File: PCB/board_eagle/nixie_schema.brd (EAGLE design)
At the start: 200 x 160 mm, 55 parts, among them IC1 LM2672M

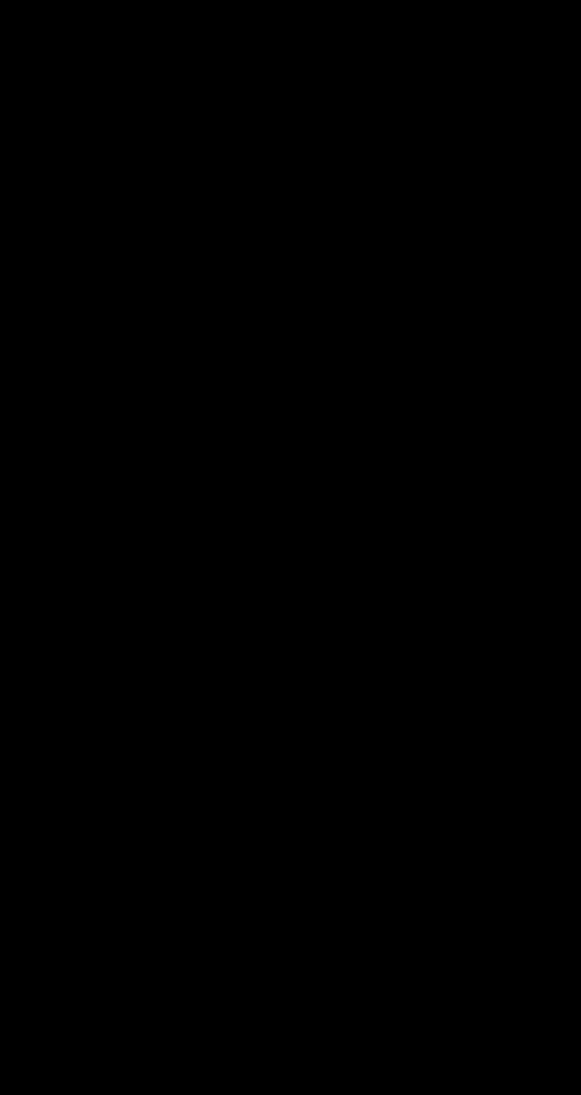
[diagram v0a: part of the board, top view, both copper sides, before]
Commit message: Fixing minor schematic issues (anode resistors and cap values in 3v3 PSU). Updated gitignore with EAGLE temp files
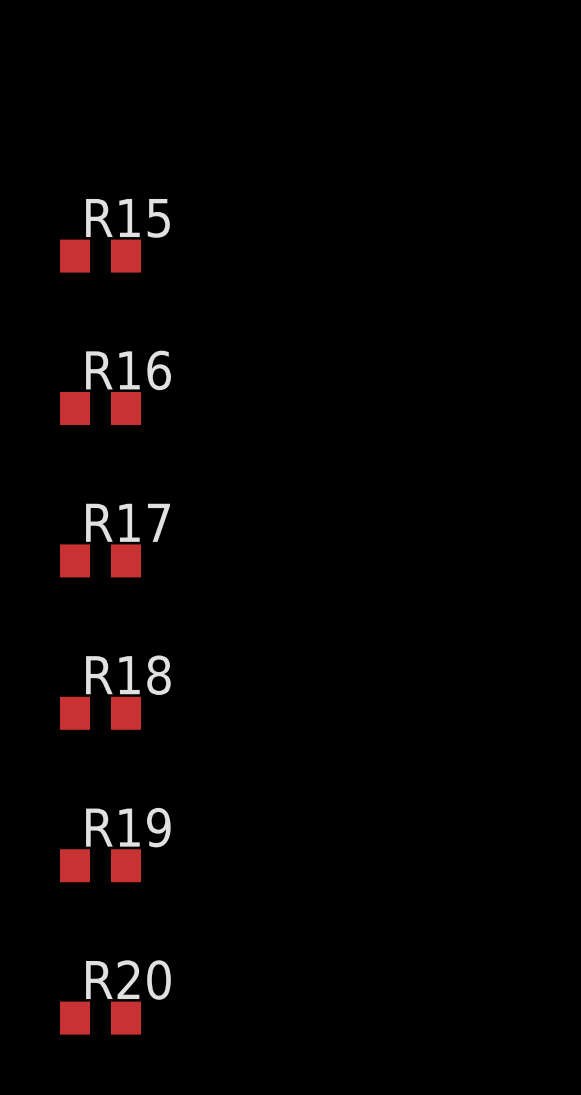
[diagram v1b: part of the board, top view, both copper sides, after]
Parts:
- added R15, R16, R17, R18, R19, R20: (no value), resistor:R0603
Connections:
- removed net N$74: N1.A, N2.A, N3.A, N4.A, N5.A, N6.A, SV10.11, SV10.12, SV11.11, SV11.12, SV12.11, SV12.12, SV7.11, SV7.12, SV8.11, SV8.12, SV9.11, SV9.12
- new net N$45: R15.2, R16.2, R17.2, R18.2, R19.2, R20.2, SV10.11, SV10.12, SV11.11, SV11.12, SV12.11, SV12.12, SV7.11, SV7.12, SV8.11, SV8.12, SV9.11, SV9.12
- new net N$89: N6.A, R20.1
- new net N$90: N5.A, R19.1
- new net N$91: N4.A, R18.1
- new net N$92: N3.A, R17.1
- new net N$93: N2.A, R16.1
- new net N$94: N1.A, R15.1
- net GND: now also C6.1; no longer C5.1
- net N$11: now also C5.1; no longer C6.1
- net N$12: now also C5.2; no longer C6.2
- net N$5: now also C6.2; no longer C5.2

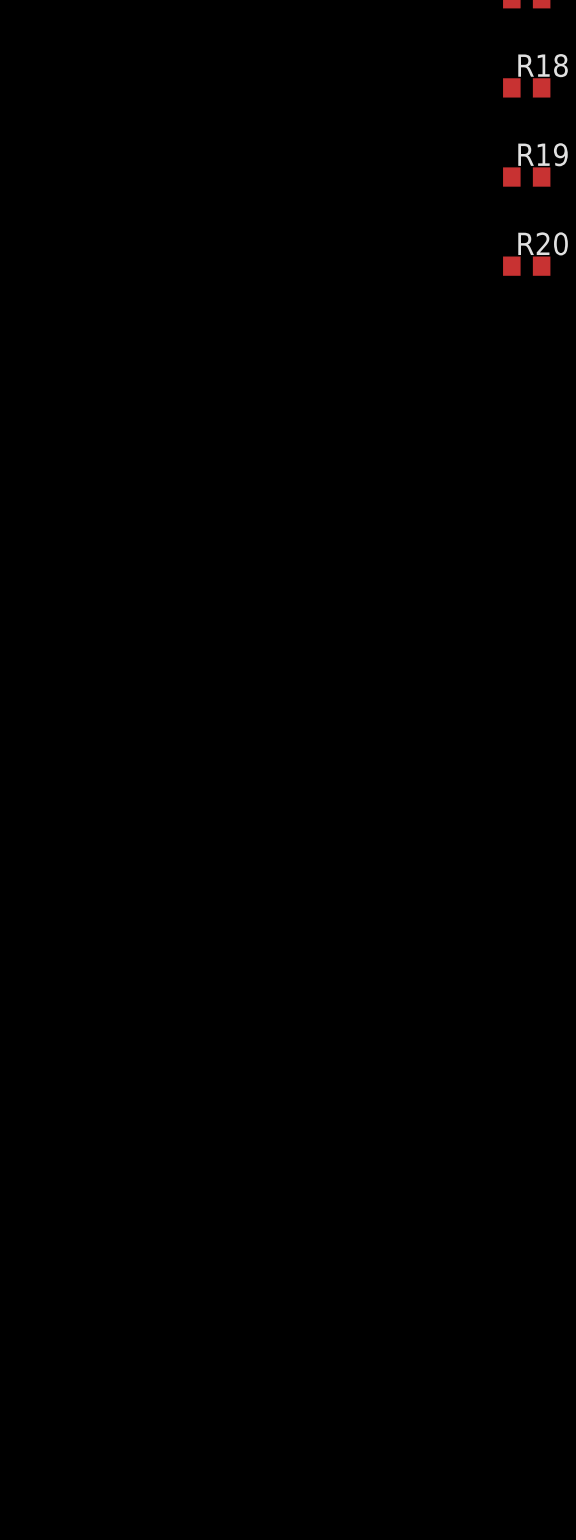
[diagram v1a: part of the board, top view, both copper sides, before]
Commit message: Most of HV supply schematic done. Need to pick transistors, caps and diode
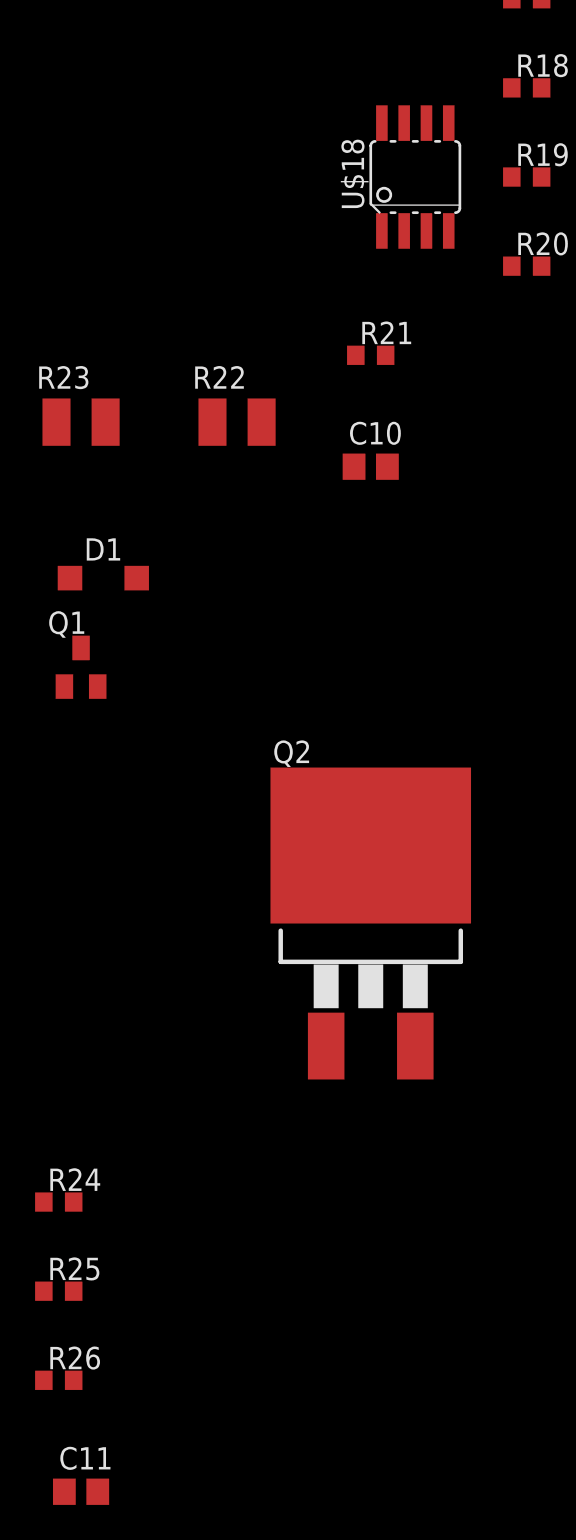
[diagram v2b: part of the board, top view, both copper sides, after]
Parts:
- added C10, C11: 680p, eagle-ltspice:C0805
- added D1: (no value), diode:SOD123
- added Q1: (no value), semicon-smd-ipc:SOT23
- added Q2: IRF3704S, transistor-power:D2PACK
- added R21: 1k, resistor:R0603
- added R22, R23: (no value), eagle-ltspice:R1210
- added R24: 330k, resistor:R0603
- added R25: 3.3k, resistor:R0603
- added R26: 5.6k, resistor:R0603
- added U$18: MC34063, MC34063:SOIC08
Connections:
- new net N$74: C10.1, U$18.3
- new net N$85: D1.A, Q1.1, R21.1, U$18.2
- new net N$86: Q2.2
- new net N$87: R22.2, R23.2, U$18.1, U$18.7, U$18.8
- new net N$95: D1.C, Q1.2, Q2.1
- new net N$96: C11.1, R24.2, R25.1, R26.1, U$18.5
- new net N$97: R26.2
- net GND: now also C10.2, C11.2, Q1.3, Q2.3, R21.2, R25.2, U$18.4
- net HV_IN+: now also R24.1
- net VCC: now also R22.1, R23.1, U$18.6

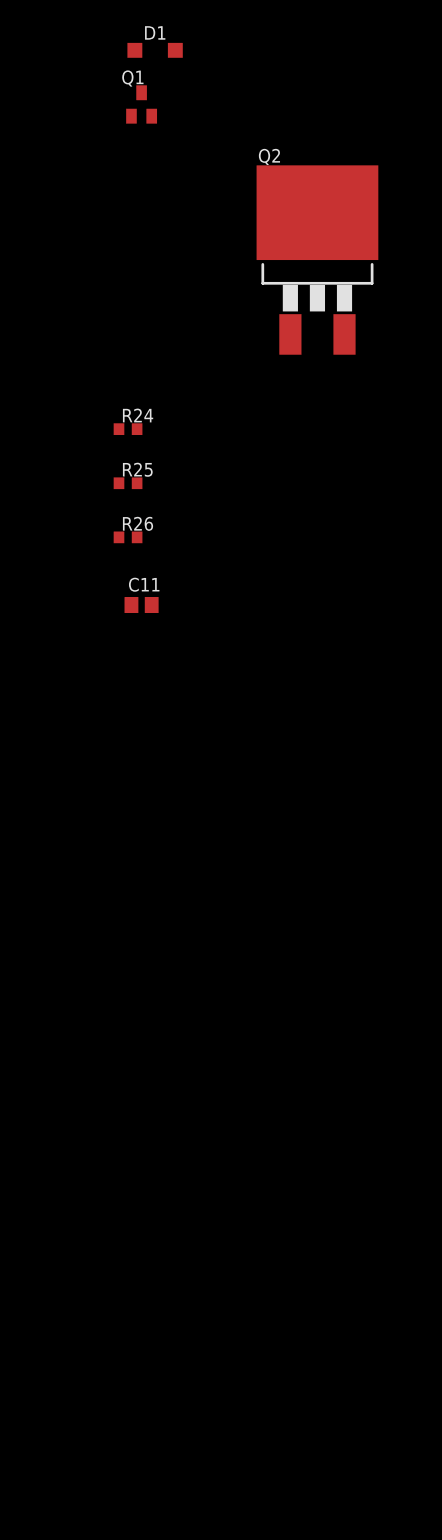
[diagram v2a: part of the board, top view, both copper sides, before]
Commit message: HV PSU schematic captured. Still need to pick correct pot
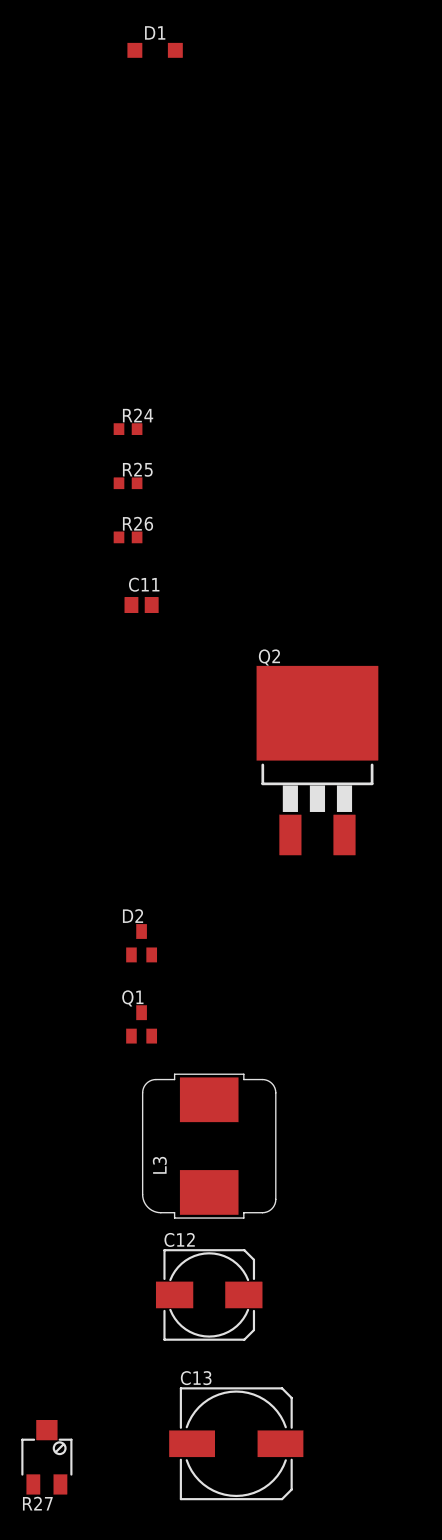
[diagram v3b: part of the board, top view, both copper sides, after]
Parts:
- added C12: 220u, rcl:153CLV-0810
- added C13: 2.2u, rcl:153CLV-1014
- added D2: BAS21, nixe_cmp:SOT23
- added L3: 150u, nixe_cmp:INDUCTOR_PACKAGE
- added R27: 100k, pot:SM-42/43X
- Q1: value (none) -> BC856B; device semicon-smd-ipc:SOT23 -> nixe_cmp:SOT23
- Q2: value IRF3704S -> IRF740S; device transistor-power:D2PACK -> nixe_cmp:D2PACK
- moved Q1 86.4 mm to (-106.7, -222.2)
- moved Q2 47.0 mm to (-90.2, -195.6)
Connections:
- net GND: now also C12.-, C13.-, R27.2
- net HV_IN+: now also C13.+, D2.3
- net N$86: now also D2.1, L3.P$2
- net N$87: now also C12.+, L3.P$1
- net N$97: now also R27.3
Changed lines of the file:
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@@
 </element>
 <element name="D1" library="diode" package="SOD123" value="" x="-105.41" y="-130.81"/>
-<element name="Q1" library="semicon-smd-ipc" package="SOT23" value="" x="-106.68" y="-135.89"/>
-<element name="Q2" library="transistor-power" package="D2PACK" value="IRF3704S" x="-90.17" y="-148.59"/>
 <element name="R24" library="resistor" package="R0603" value="330k" x="-107.95" y="-166.37"/>
 <element name="R25" library="resistor" package="R0603" value="3.3k" x="-107.95" y="-171.45"/>
@@
 <attribute name="SPICEPREFIX" value="C" x="-106.68" y="-182.88" size="1.778" layer="27" display="off"/>
 </element>
+<element name="Q2" library="nixe_cmp" package="D2PACK" value="IRF740S" x="-90.17" y="-195.58"/>
+<element name="D2" library="nixe_cmp" package="SOT23" value="BAS21" x="-106.68" y="-214.63"/>
+<element name="Q1" library="nixe_cmp" package="SOT23" value="BC856B" x="-106.68" y="-222.25"/>
+<element name="L3" library="nixe_cmp" package="INDUCTOR_PACKAGE" value="150u" x="-100.33" y="-233.68"/>
+<element name="C12" library="rcl" package="153CLV-0810" value="220u" x="-100.33" y="-247.65"/>
+<element name="C13" library="rcl" package="153CLV-1014" value="2.2u" x="-97.79" y="-261.62"/>
+<element name="R27" library="pot" package="SM-42/43X" value="100k" x="-115.57" y="-262.89"/>
 </elements>
 <signals>
@@
 <contactref element="C10" pad="2"/>
 <contactref element="R21" pad="2"/>
-<contactref element="Q1" pad="3"/>
-<contactref element="Q2" pad="3"/>
 <contactref element="R25" pad="2"/>
 <contactref element="C11" pad="2"/>
-<wire x1="-107.1" y1="-171.45" x2="-87.63" y2="-157.48" width="0" layer="19" extent="1-1"/>
-<wire x1="-105.73" y1="-182.88" x2="-107.1" y2="-171.45" width="0" layer="19" extent="1-1"/>
-<wire x1="-106.68" y1="-134.79" x2="-87.63" y2="-157.48" width="0" layer="19" extent="1-1"/>
-<wire x1="-89.22" y1="-124.46" x2="-106.68" y2="-134.79" width="0" layer="19" extent="1-1"/>
+<contactref element="Q2" pad="3"/>
+<contactref element="Q1" pad="3"/>
+<contactref element="C12" pad="-"/>
+<contactref element="C13" pad="-"/>
+<contactref element="R27" pad="2"/>
 <wire x1="-89.32" y1="-118.11" x2="-89.22" y2="-124.46" width="0" layer="19" extent="1-1"/>
 <wire x1="-85.725" y1="-111.0234" x2="-89.32" y2="-118.11" width="0" layer="19" extent="1-1"/>
+<wire x1="-107.1" y1="-171.45" x2="-89.22" y2="-124.46" width="0" layer="19" extent="1-1"/>
+<wire x1="-105.73" y1="-182.88" x2="-107.1" y2="-171.45" width="0" layer="19" extent="1-1"/>
+<wire x1="-87.63" y1="-204.47" x2="-105.73" y2="-182.88" width="0" layer="19" extent="1-1"/>
+<wire x1="-106.68" y1="-221.15" x2="-87.63" y2="-204.47" width="0" layer="19" extent="1-1"/>
+<wire x1="-103.58" y1="-247.65" x2="-106.68" y2="-221.15" width="0" layer="19" extent="1-1"/>
+<wire x1="-101.94" y1="-261.62" x2="-103.58" y2="-247.65" width="0" layer="19" extent="1-1"/>
+<wire x1="-115.57" y1="-260.34" x2="-101.94" y2="-261.62" width="0" layer="19" extent="1-1"/>
 <wire x1="-76.91" y1="55.88" x2="-85.725" y2="-111.0234" width="0" layer="19" extent="1-1"/>
 <wire x1="-64.21" y1="55.88" x2="-76.91" y2="55.88" width="0" layer="19" extent="1-1"/>
@@
 <contactref element="SV6" pad="12"/>
 <contactref element="R24" pad="1"/>
+<contactref element="D2" pad="3"/>
+<contactref element="C13" pad="+"/>
 <wire x1="186.35" y1="58.73" x2="186.35" y2="61.27" width="0" layer="19" extent="1-1"/>
 <wire x1="166.35" y1="61.27" x2="186.35" y2="61.27" width="0" layer="19" extent="1-1"/>
@@
 <wire x1="26.35" y1="58.73" x2="26.35" y2="61.27" width="0" layer="19" extent="1-1"/>
 <wire x1="-108.8" y1="-166.37" x2="26.35" y2="58.73" width="0" layer="19" extent="1-1"/>
+<wire x1="-106.68" y1="-213.53" x2="-108.8" y2="-166.37" width="0" layer="19" extent="1-1"/>
+<wire x1="-93.64" y1="-261.62" x2="-106.68" y2="-213.53" width="0" layer="19" extent="1-1"/>
 </signal>
 <signal name="HV_HA_0">
@@
 <contactref element="D1" pad="A"/>
 <contactref element="Q1" pad="1"/>
-<wire x1="-103.51" y1="-130.81" x2="-107.63" y2="-136.99" width="0" layer="19" extent="1-1"/>
 <wire x1="-91.02" y1="-118.11" x2="-103.51" y2="-130.81" width="0" layer="19" extent="1-1"/>
 <wire x1="-88.265" y1="-111.0234" x2="-91.02" y2="-118.11" width="0" layer="19" extent="1-1"/>
+<wire x1="-107.63" y1="-223.35" x2="-103.51" y2="-130.81" width="0" layer="19" extent="1-1"/>
 </signal>
 <signal name="N$87">
@@
 <contactref element="U$18" pad="8"/>
 <contactref element="U$18" pad="1"/>
+<contactref element="L3" pad="P$1"/>
+<contactref element="C12" pad="+"/>
 <wire x1="-96.39" y1="-121.92" x2="-105.28" y2="-121.92" width="0" layer="19" extent="1-1"/>
 <wire x1="-89.535" y1="-111.0234" x2="-96.39" y2="-121.92" width="0" layer="19" extent="1-1"/>
 <wire x1="-89.535" y1="-104.8766" x2="-89.535" y2="-111.0234" width="0" layer="19" extent="1-1"/>
 <wire x1="-88.265" y1="-104.8766" x2="-89.535" y2="-104.8766" width="0" layer="19" extent="1-1"/>
+<wire x1="-100.33" y1="-229.33" x2="-96.39" y2="-121.92" width="0" layer="19" extent="1-1"/>
+<wire x1="-97.08" y1="-247.65" x2="-100.33" y2="-229.33" width="0" layer="19" extent="1-1"/>
 </signal>
 <signal name="N$95">
-<contactref element="Q1" pad="2"/>
 <contactref element="D1" pad="C"/>
 <contactref element="Q2" pad="1"/>
-<wire x1="-105.73" y1="-136.99" x2="-92.71" y2="-157.48" width="0" layer="19" extent="1-1"/>
-<wire x1="-107.31" y1="-130.81" x2="-105.73" y2="-136.99" width="0" layer="19" extent="1-1"/>
+<contactref element="Q1" pad="2"/>
+<wire x1="-92.71" y1="-204.47" x2="-107.31" y2="-130.81" width="0" layer="19" extent="1-1"/>
+<wire x1="-105.73" y1="-223.35" x2="-92.71" y2="-204.47" width="0" layer="19" extent="1-1"/>
 </signal>
 <signal name="N$96">
@@
 <wire x1="-107.63" y1="-182.88" x2="-108.8" y2="-176.53" width="0" layer="19" extent="1-1"/>
 </signal>
+<signal name="N$97">
+<contactref element="R26" pad="2"/>
+<contactref element="R27" pad="3"/>
+<wire x1="-107.1" y1="-176.53" x2="-114.3" y2="-265.44" width="0" layer="19" extent="1-1"/>
+</signal>
 <signal name="N$86">
 <contactref element="Q2" pad="2"/>
-</signal>
-<signal name="N$97">
-<contactref element="R26" pad="2"/>
+<contactref element="D2" pad="1"/>
+<contactref element="L3" pad="P$2"/>
+<wire x1="-107.63" y1="-215.73" x2="-100.33" y2="-238.03" width="0" layer="19" extent="1-1"/>
+<wire x1="-90.17" y1="-193.04" x2="-107.63" y2="-215.73" width="0" layer="19" extent="1-1"/>
 </signal>
 </signals>

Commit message: Added Buttons
Added 4 buttons and two strip for connectors. buttons are on the last
alb gpios. removed connections for DOT_LED
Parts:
- added J3: (no value), SparkFun-Connectors:1X06_NO_SILK
- added R28, R29, R30: 2.21K, rcl:R0603
- added S2, S3, S4, S5: TAC_SWITCHSMD, SparkFun-Retired:TACTILE-SWITCH-SMD
- J2: device SparkFun-Connectors:1X03 -> SparkFun-Connectors:1X06_NO_SILK
- R7: value 150 -> 2.21K
- moved J2 430.5 mm to (-109.2, -344.2), turned to 0 degrees
- moved R7 408.5 mm to (-116.8, -316.2)
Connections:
- removed net DOT_LED: R7.1, U$13.G4
- removed net N$10: J2.2, R7.2
- removed net N$19: U$13.G12
- removed net N$21: U$13.G13
- new net BUTTON1: J2.2, J3.2, R30.2, S5.1, S5.2, U$13.G4
- new net BUTTON2: J2.3, J3.3, R29.2, S4.1, S4.2, U$13.G2
- new net BUTTON3: J2.4, J3.4, R28.2, S3.1, S3.2, U$13.G12
- new net BUTTON4: J2.5, J3.5, R7.2, S2.1, S2.2, U$13.G13
- net +3V3: now also J3.1, S2.3, S3.3, S4.3, S5.3
- net GND: now also J2.6, J3.6, R28.1, R29.1, R30.1, R7.1; no longer J2.3

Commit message: Changed ESP8266
changed esp8266 footprint
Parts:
- removed U$13: ESP8266-07-12, PatternAgents_RFmodules:ESP8266-07W
- added U1: (no value), PatternAgents_RFmodules:ESP12E-SMD
- S1: value MOMENTARY-SWITCH-SPST-SMD-4.5MM -> TAC_SWITCHSMD; device SparkFun-Switches:TACTILE_SWITCH_SMD_4.5MM -> SparkFun-Retired:TACTILE-SWITCH-SMD
- moved S1 438.6 mm to (-113.0, -356.9)
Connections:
- net +3V3: now also U1.VCC; no longer U$13.VCC
- net BUTTON1: now also U1.GPIO5; no longer U$13.G4
- net BUTTON2: now also U1.GPIO2; no longer U$13.G2
- net BUTTON3: now also U1.GPIO12; no longer U$13.G12
- net BUTTON4: now also U1.GPIO13; no longer U$13.G13
- net DATA_CLK: now also U1.GPIO14; no longer U$13.G14
- net DATA_IN: now also U1.GPIO16; no longer U$13.G16
- net GND: now also U1.GND; no longer S1.3, U$13.GND
- net LE: now also U1.GPIO4; no longer U$13.G5
- net N$14: now also U1.RESET; no longer S1.1, U$13.!RST
- net N$16: now also U1.CH_PD; no longer U$13.CH_PD
- net N$17: now also U1.TXD0; no longer U$13.TXD
- net N$18: now also U1.RXD0; no longer U$13.RXD
- net N$20: now also U1.GPIO15; no longer U$13.G15
- net N$22: now also U1.GPIO0; no longer U$13.G0

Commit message: Brought Anode resistors to the lower PCB
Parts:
- R15, R16, R17, R18, R19, R20: value (none) -> 10k; device resistor:R0603 -> rcl:R0603
- moved R20 281.3 mm to (-143.5, -387.4)
- moved R15 281.3 mm to (-143.5, -361.9)
- moved R16 281.3 mm to (-143.5, -367.0)
- moved R17 281.3 mm to (-143.5, -372.1)
- moved R18 281.3 mm to (-143.5, -377.2)
- moved R19 281.3 mm to (-143.5, -382.3)
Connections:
- new net N$10: N1.A, SV7.11, SV7.12
- new net N$100: R18.2
- new net N$101: R17.2
- new net N$102: R16.2
- new net N$19: N2.A, SV8.11, SV8.12
- new net N$21: N3.A, SV9.11, SV9.12
- new net N$88: N4.A, SV10.11, SV10.12
- new net N$98: N5.A, SV11.11, SV11.12
- new net N$99: R19.2
- net HV_IN+: now also R17.1, R18.1; no longer SV1.11, SV1.12, SV2.11, SV2.12, SV5.11, SV5.12, SV6.11, SV6.12
- net N$45: now also N6.A; no longer R15.2, R16.2, R17.2, R18.2, R19.2, R20.2, SV10.11, SV10.12, SV11.11, SV11.12, SV7.11, SV7.12, SV8.11, SV8.12, SV9.11, SV9.12
- net N$89: now also R15.1, SV1.11, SV1.12; no longer N6.A, R20.1
- net N$90: now also R16.1, SV2.11, SV2.12; no longer N5.A, R19.1
- net N$91: now also R20.1, SV6.11, SV6.12; no longer N4.A, R18.1
- net N$92: now also R19.1, SV5.11, SV5.12; no longer N3.A, R17.1
- net N$93: now also R15.2; no longer N2.A, R16.1
- net N$94: now also R20.2; no longer N1.A, R15.1
